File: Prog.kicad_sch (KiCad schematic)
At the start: 26 parts, among them J2 JTAG, J3 microUSB, Q1 MMBT3904, Q2 MMBT3904, U12 CH340G, U25 74LVC245APW, Y1 12M

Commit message: RC
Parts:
- removed C21: 2u2, stdpads:C_0603, symbol Device:C_Small
- removed Q2: MMBT3904, stdpads:SOT-23, symbol Transistor_BJT:MMBT3904
- removed R13, R14, R8: 1k, stdpads:R_0603, symbol Device:R_Small
- removed R9: 10k, stdpads:R_0603, symbol Device:R_Small
- removed U25: 74LVC245APW, stdpads:TSSOP-20_4.4x6.5mm_P0.65mm, symbol GW_Logic:74245
- J3: footprint stdpads:USB_Micro-B_ShouHan_MicroXNJ -> stdpads:USB_Micro-B_Amphenol_10118192-0001
- renumbered R2 to R20, R2 to R23
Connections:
- net JTAG~{OE} is gone; now on an unnamed net: Q1.3 (C)
- net TCKru is gone; now on net UTCK: R20.1
- net UTDI is gone; now on net TDI: U12.13 (~{DTR})
- net UTDO is gone; now on net TDO: U12.9 (~{CTS})
- net UTMS is gone; now on net TMS: U12.14 (~{RTS})
- net +3V3: now also U12.3 (RXD)
- net at R10.2, R11.1: now also Q1.1 (B)
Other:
- company: (none) -> Garrett's Workshop
- title: (none) -> WarpSE (GW4410A)
- moved on the sheet: C23, C25, R20

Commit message: RC
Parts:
- J2: footprint Connector:Tag-Connect_TC2050-IDC-FP_2x05_P1.27mm_Vertical -> stdpads:Tag-Connect_TC2050-IDC-FP_2x05_P1.27mm_Vertical
- J3: LCSC Part C404969 -> C132564
- R10, R11: LCSC Part (none) -> C21190
- R15, R16: value 10k -> DNP; LCSC Part C25804 -> (none)
- R19: LCSC Part (none) -> C23182
- Y1: LCSC Part (none) -> C9002
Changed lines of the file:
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@@
   (title_block
     (title "WarpSE (GW4410A)")
-    (date "2024-03-27")
+    (date "2024-04-23")
     (rev "1.0")
     (company "Garrett's Workshop")
@@
       (effects (font (size 1.27 1.27)))
     )
-    (property "Footprint" "Connector:Tag-Connect_TC2050-IDC-FP_2x05_P1.27mm_Vertical" (at 107.95 57.15 0)
-      (effects (font (size 1.27 1.27)) hide)
-    )
-    (property "Datasheet" "~" (at 107.95 57.15 0)
+    (property "Footprint" "stdpads:Tag-Connect_TC2050-IDC-FP_2x05_P1.27mm_Vertical" (at 107.95 57.15 0)
+      (effects (font (size 1.27 1.27)) hide)
+    )
+    (property "Datasheet" "" (at 107.95 57.15 0)
       (effects (font (size 1.27 1.27)) hide)
     )
@@
       (effects (font (size 1.27 1.27)) (justify left) hide)
     )
-    (property "Datasheet" "http://www.datasheet5.com/pdf-local-2195953" (at 229.87 39.37 0)
+    (property "Datasheet" "" (at 229.87 39.37 0)
       (effects (font (size 1.27 1.27)) hide)
     )
@@
       (effects (font (size 1.27 1.27)) hide)
     )
-    (property "Datasheet" "~" (at 209.55 143.51 0)
+    (property "Datasheet" "" (at 209.55 143.51 0)
       (effects (font (size 1.27 1.27)) hide)
     )
@@
       (effects (font (size 1.27 1.27)) hide)
     )
-    (property "Datasheet" "~" (at 219.71 143.51 0)
+    (property "Datasheet" "" (at 219.71 143.51 0)
       (effects (font (size 1.27 1.27)) hide)
     )
@@
       (effects (font (size 1.27 1.27)) hide)
     )
-    (property "Datasheet" "~" (at 229.87 143.51 0)
+    (property "Datasheet" "" (at 229.87 143.51 0)
       (effects (font (size 1.27 1.27)) hide)
     )
@@
       (effects (font (size 1.27 1.27)) hide)
     )
-    (property "Datasheet" "~" (at 240.03 72.39 0)
+    (property "Datasheet" "" (at 240.03 72.39 0)
       (effects (font (size 1.27 1.27)) hide)
     )
@@
       (effects (font (size 1.27 1.27)) hide)
     )
-    (property "Datasheet" "~" (at 250.19 72.39 0)
+    (property "Datasheet" "" (at 250.19 72.39 0)
       (effects (font (size 1.27 1.27)) hide)
     )
@@
       (effects (font (size 1.27 1.27)) hide)
     )
-    (property "Datasheet" "~" (at 255.27 58.42 0)
-      (effects (font (size 1.27 1.27)) hide)
-    )
-    (property "LCSC Part" "C404969" (at 259.08 57.15 0)
+    (property "Datasheet" "" (at 255.27 58.42 0)
+      (effects (font (size 1.27 1.27)) hide)
+    )
+    (property "LCSC Part" "C132564" (at 259.08 57.15 0)
       (effects (font (size 1.27 1.27)) hide)
     )
@@
       (effects (font (size 1.27 1.27)) (justify right))
     )
-    (property "Value" "10k" (at 73.66 62.23 0)
+    (property "Value" "DNP" (at 73.66 62.23 0)
       (effects (font (size 1.27 1.27)) (justify right))
     )
@@
       (effects (font (size 1.27 1.27)) hide)
     )
-    (property "Datasheet" "~" (at 72.39 60.96 0)
-      (effects (font (size 1.27 1.27)) hide)
-    )
-    (property "LCSC Part" "C25804" (at 72.39 60.96 0)
+    (property "Datasheet" "" (at 72.39 60.96 0)
+      (effects (font (size 1.27 1.27)) hide)
+    )
+    (property "LCSC Part" "" (at 72.39 60.96 0)
       (effects (font (size 1.27 1.27)) hide)
     )
@@
       (effects (font (size 1.27 1.27)) (justify right))
     )
-    (property "Value" "10k" (at 73.66 54.61 0)
+    (property "Value" "DNP" (at 73.66 54.61 0)
       (effects (font (size 1.27 1.27)) (justify right))
     )
@@
       (effects (font (size 1.27 1.27)) hide)
     )
-    (property "Datasheet" "~" (at 72.39 53.34 0)
-      (effects (font (size 1.27 1.27)) hide)
-    )
-    (property "LCSC Part" "C25804" (at 72.39 53.34 0)
+    (property "Datasheet" "" (at 72.39 53.34 0)
+      (effects (font (size 1.27 1.27)) hide)
+    )
+    (property "LCSC Part" "" (at 72.39 53.34 0)
       (effects (font (size 1.27 1.27)) hide)
     )
@@
       (effects (font (size 1.27 1.27)) hide)
     )
-    (property "Datasheet" "~" (at 240.03 102.87 0)
-      (effects (font (size 1.27 1.27)) hide)
-    )
-    (property "LCSC Part" "" (at 240.03 102.87 0)
+    (property "Datasheet" "" (at 240.03 102.87 0)
+      (effects (font (size 1.27 1.27)) hide)
+    )
+    (property "LCSC Part" "C21190" (at 240.03 102.87 0)
       (effects (font (size 1.27 1.27)) hide)
     )
@@
       (effects (font (size 1.27 1.27)) hide)
     )
-    (property "Datasheet" "~" (at 234.95 67.31 0)
+    (property "Datasheet" "" (at 234.95 67.31 0)
+      (effects (font (size 1.27 1.27)) hide)
+    )
+    (property "LCSC Part" "C9002" (at 234.95 67.31 90)
       (effects (font (size 1.27 1.27)) hide)
     )
@@
       (effects (font (size 1.27 1.27) italic) (justify left) hide)
     )
-    (property "Datasheet" "https://www.onsemi.com/pub/Collateral/2N3903-D.PDF" (at 224.79 105.41 0)
+    (property "Datasheet" "" (at 224.79 105.41 0)
       (effects (font (size 1.27 1.27)) (justify left) hide)
     )
@@
       (effects (font (size 1.27 1.27)) hide)
     )
-    (property "Datasheet" "~" (at 198.12 49.53 0)
+    (property "Datasheet" "" (at 198.12 49.53 0)
       (effects (font (size 1.27 1.27)) hide)
     )
@@
       (effects (font (size 1.27 1.27)) hide)
     )
-    (property "Datasheet" "~" (at 222.25 97.79 0)
-      (effects (font (size 1.27 1.27)) hide)
-    )
-    (property "LCSC Part" "" (at 222.25 97.79 0)
+    (property "Datasheet" "" (at 222.25 97.79 0)
+      (effects (font (size 1.27 1.27)) hide)
+    )
+    (property "LCSC Part" "C23182" (at 222.25 97.79 0)
       (effects (font (size 1.27 1.27)) hide)
     )
@@
       (effects (font (size 1.27 1.27)) hide)
     )
-    (property "Datasheet" "~" (at 199.39 143.51 0)
+    (property "Datasheet" "" (at 199.39 143.51 0)
       (effects (font (size 1.27 1.27)) hide)
     )
@@
       (effects (font (size 1.27 1.27)) hide)
     )
-    (property "Datasheet" "~" (at 95.25 52.07 0)
+    (property "Datasheet" "" (at 95.25 52.07 0)
       (effects (font (size 1.27 1.27)) hide)
     )
@@
       (effects (font (size 1.27 1.27)) hide)
     )
-    (property "Datasheet" "~" (at 240.03 107.95 0)
-      (effects (font (size 1.27 1.27)) hide)
-    )
-    (property "LCSC Part" "" (at 240.03 107.95 0)
+    (property "Datasheet" "" (at 240.03 107.95 0)
+      (effects (font (size 1.27 1.27)) hide)
+    )
+    (property "LCSC Part" "C21190" (at 240.03 107.95 0)
       (effects (font (size 1.27 1.27)) hide)
     )
@@
       (effects (font (size 1.27 1.27)) hide)
     )
-    (property "Datasheet" "~" (at 80.01 60.96 0)
-      (effects (font (size 1.27 1.27)) hide)
-    )
+    (property "Datasheet" "" (at 80.01 60.96 0)
+      (effects (font (size 1.27 1.27)) hide)
+    )

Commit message: USB power
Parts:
- added D1: 1N5819, symbol Device:D_Schottky_Small_Filled
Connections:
- net USB5V: now also D1.2 (A)
- new net +5V: D1.1 (K)

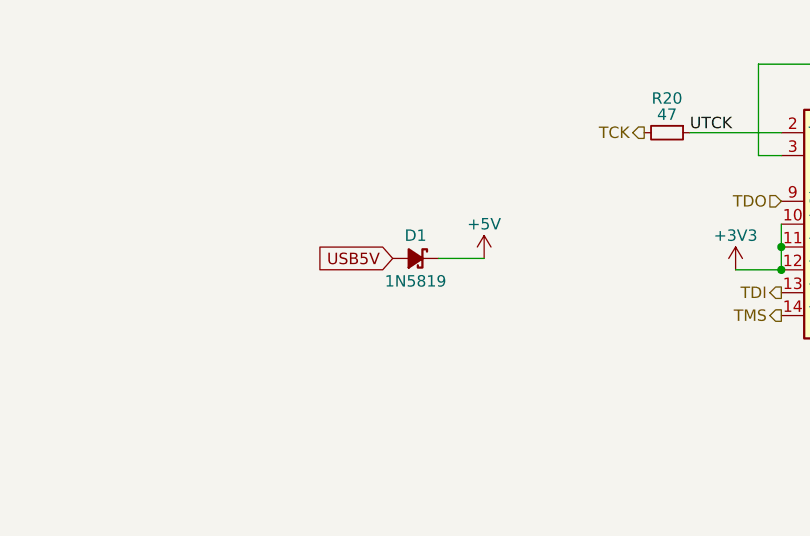
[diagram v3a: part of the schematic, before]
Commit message: Add LM66100 instead of MAX40200AUK
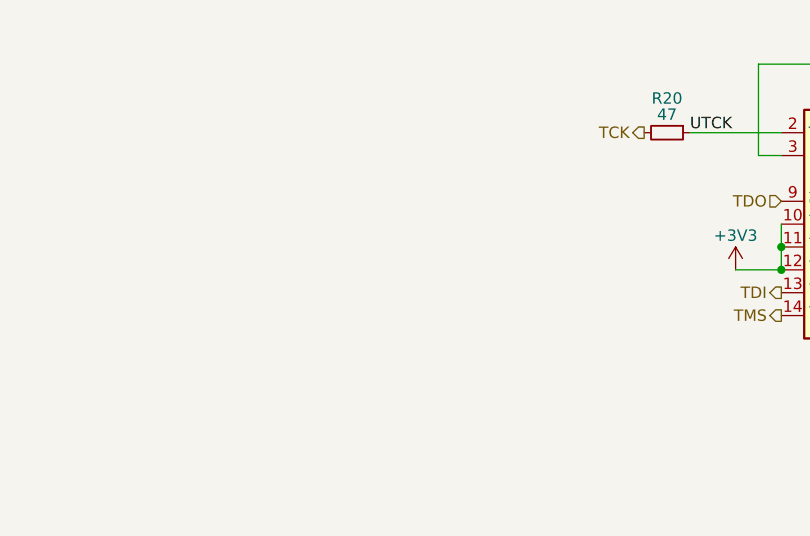
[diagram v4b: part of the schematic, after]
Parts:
- removed D1: 1N5819, symbol Device:D_Schottky_Small_Filled
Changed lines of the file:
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@@
-	(wire
-		(pts
-			(xy 172.72 63.5) (xy 177.8 63.5)
-		)
-		(stroke
-			(width 0)
-			(type default)
-		)
-	)
 	(wire
 		(pts
@@
 	(global_label "USB5V"
 		(shape input)
-		(at 167.64 63.5 180)
-		(fields_autoplaced yes)
-		(effects
-			(font
-				(size 1.27 1.27)
-			)
-			(justify right)
-		)
-		(property "Intersheetrefs" "${INTERSHEET_REFS}"
-			(at 159.2803 63.5 0)
-			(effects
-				(font
-					(size 1.27 1.27)
-				)
-				(justify right)
-				(hide yes)
-			)
-		)
-	)
-	(global_label "USB5V"
-		(shape input)
 		(at 228.6 139.7 180)
 		(fields_autoplaced yes)
@@
 	)
 	(symbol
-		(lib_id "Device:D_Schottky_Small_Filled")
-		(at 170.18 63.5 0)
-		(mirror y)
-		(unit 1)
-		(exclude_from_sim no)
-		(in_bom yes)
-		(on_board yes)
-		(dnp no)
-		(property "Reference" "D1"
-			(at 170.18 60.96 0)
-			(effects
-				(font
-					(size 1.27 1.27)
-				)
-			)
-		)
-		(property "Value" "1N5819"
-			(at 170.18 66.04 0)
-			(effects
-				(font
-					(size 1.27 1.27)
-				)
-			)
-		)
-		(property "Footprint" ""
-			(at 170.18 63.5 90)
-			(effects
-				(font
-					(size 1.27 1.27)
-				)
-				(hide yes)
-			)
-		)
-		(property "Datasheet" "~"
-			(at 170.18 63.5 90)
-			(effects
-				(font
-					(size 1.27 1.27)
-				)
-				(hide yes)
-			)
-		)
-		(property "Description" "Schottky diode, small symbol, filled shape"
-			(at 170.18 63.5 0)
-			(effects
-				(font
-					(size 1.27 1.27)
-				)
-				(hide yes)
-			)
-		)
-		(pin "2"
-		)
-		(pin "1"
-		)
-		(instances
-			(project ""
-				(path "/a5be2cb8-c68d-4180-8412-69a6b4c5b1d4/00000000-0000-0000-0000-000061aa52c4"
-					(reference "D1")
-					(unit 1)
-				)
-			)
-		)
-	)
-	(symbol
 		(lib_id "Device:Crystal_GND24_Small")
 		(at 234.95 67.31 90)
@@
 					(unit 1)
 				)
-			)
-		)
-	)
-	(symbol
-		(lib_id "power:+5V")
-		(at 177.8 63.5 0)
-		(unit 1)
-		(exclude_from_sim no)
-		(in_bom yes)
-		(on_board yes)
-		(dnp no)
-		(property "Reference" "#PWR031"
-			(at 177.8 67.31 0)
-			(effects
-				(font
-					(size 1.27 1.27)
-				)
-				(hide yes)
-			)
-		)
-		(property "Value" "+5V"
-			(at 177.8 59.69 0)
-			(effects
-				(font
-					(size 1.27 1.27)
-				)
-			)
-		)
-		(property "Footprint" ""
-			(at 177.8 63.5 0)
-			(effects
-				(font
-					(size 1.27 1.27)
-				)
-				(hide yes)
-			)
-		)
-		(property "Datasheet" ""
-			(at 177.8 63.5 0)
-			(effects
-				(font
-					(size 1.27 1.27)
-				)
-				(hide yes)
-			)
-		)
-		(property "Description" "Power symbol creates a global label with name \"+5V\""
-			(at 177.8 63.5 0)
-			(effects
-				(font
-					(size 1.27 1.27)
-				)
-				(hide yes)
-			)
-		)
-		(pin "1"
-		)
-		(instances
-			(project ""
-				(path "/a5be2cb8-c68d-4180-8412-69a6b4c5b1d4/00000000-0000-0000-0000-000061aa52c4"
-					(reference "#PWR031")
-					(unit 1)
-				)

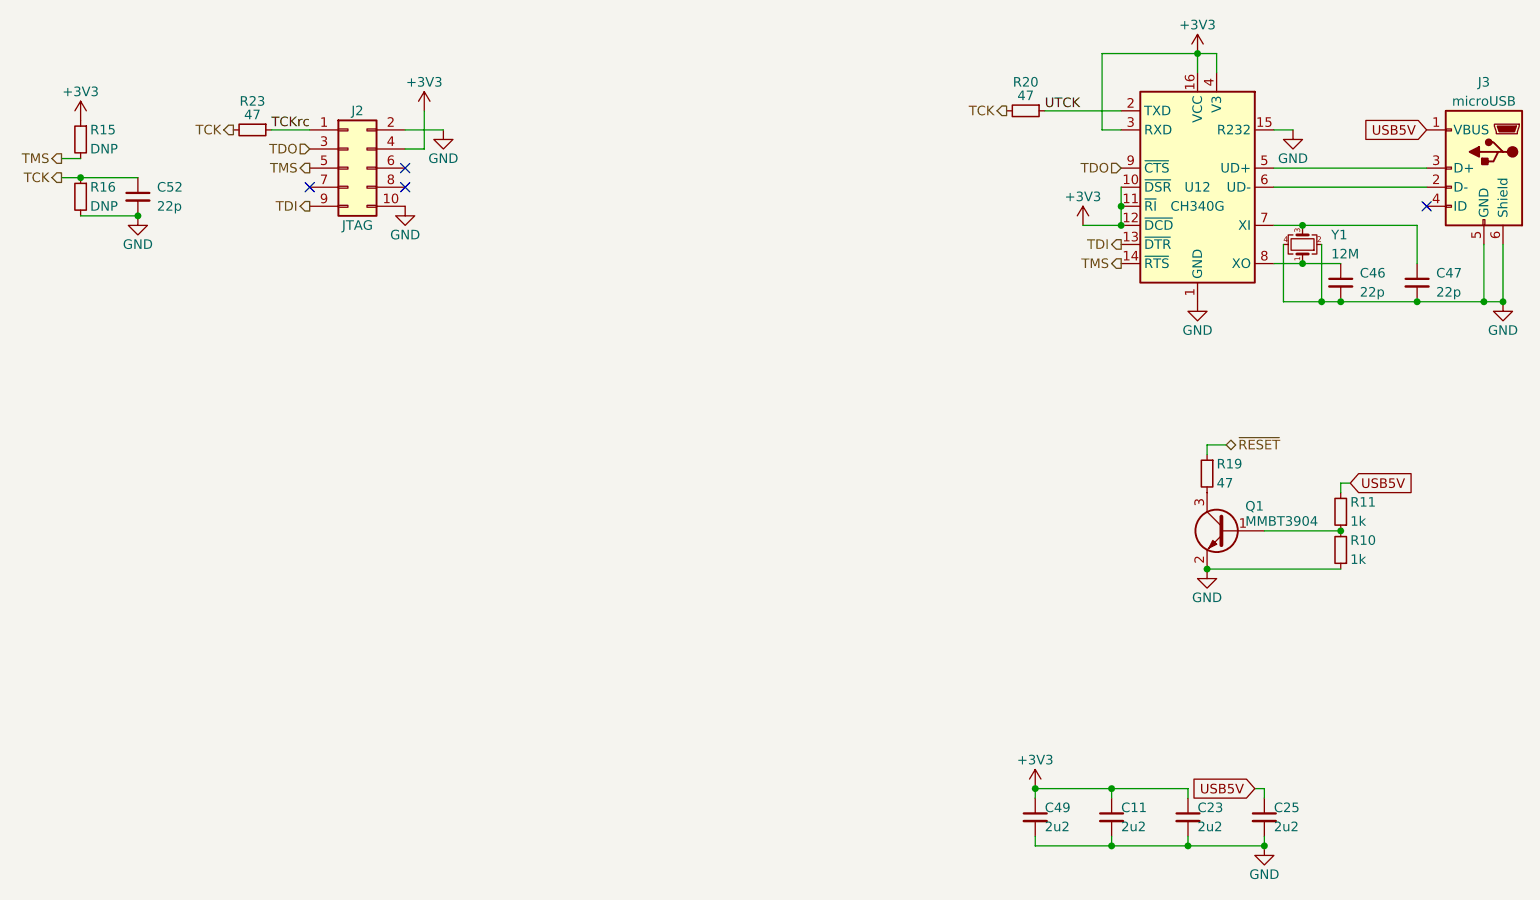
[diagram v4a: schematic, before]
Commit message: Board prerelease revision 3 with USB power, A[23:20] remapping
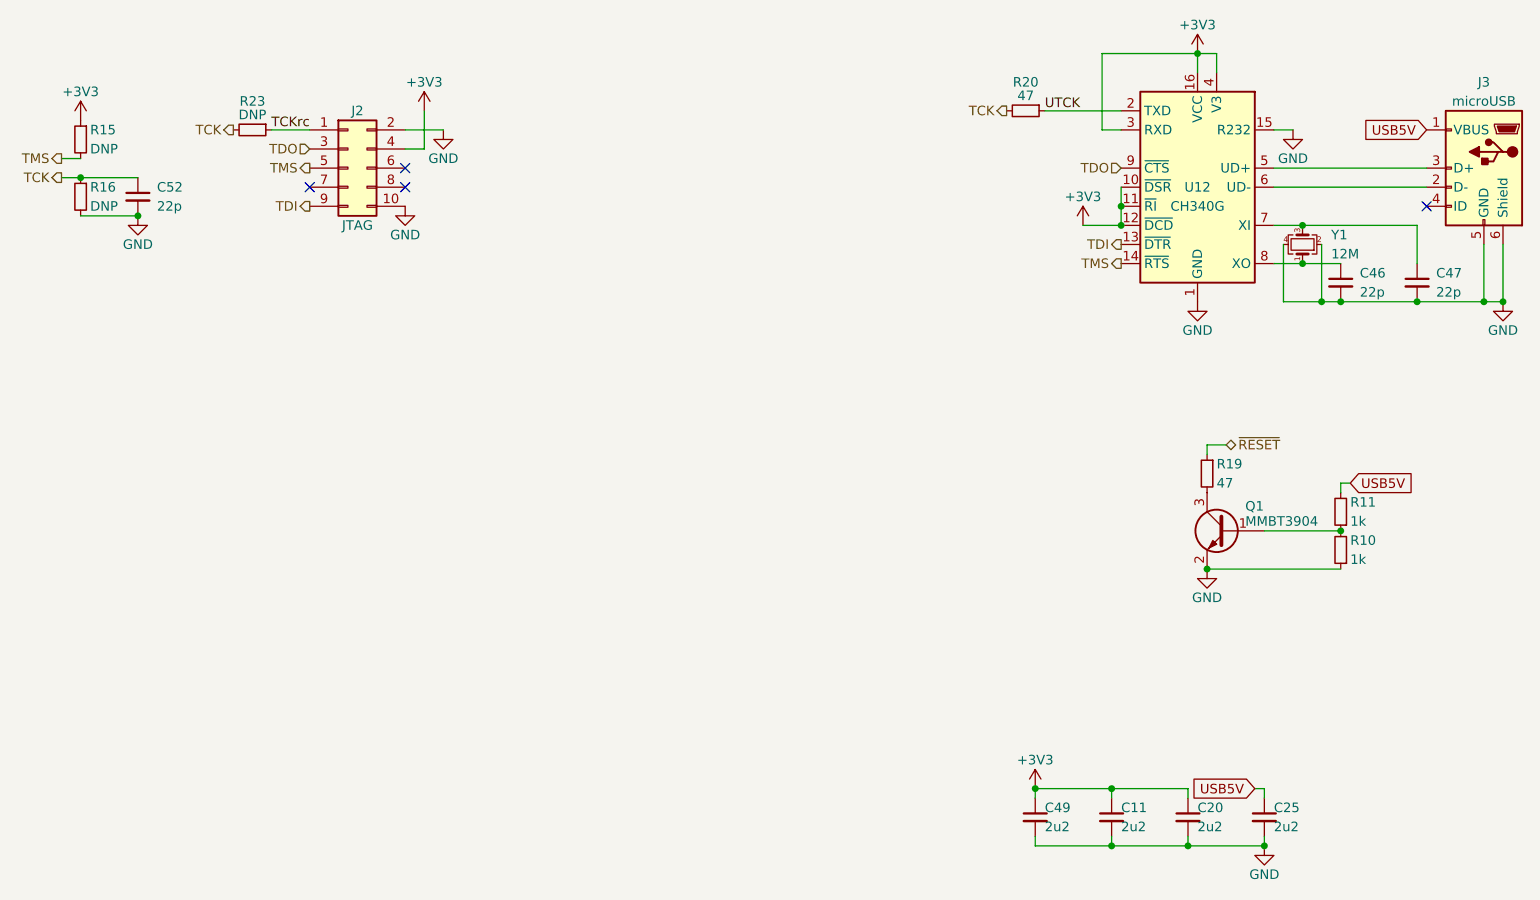
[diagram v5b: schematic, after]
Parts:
- removed C23: 2u2, stdpads:C_0603, symbol Device:C_Small
- added C20: 2u2, stdpads:C_0603, symbol Device:C_Small
- R23: value 47 -> DNP; LCSC Part C23182 -> (none)
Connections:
- net +3V3: now also C20.1
- net GND: now also C20.2
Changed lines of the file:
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@@
-	(symbol
-		(lib_id "Device:C_Small")
-		(at 219.71 143.51 0)
-		(unit 1)
-		(exclude_from_sim no)
-		(in_bom yes)
-		(on_board yes)
-		(dnp no)
-		(property "Reference" "C23"
-			(at 220.98 142.24 0)
-			(effects
-				(font
-					(size 1.27 1.27)
-				)
-				(justify left)
-			)
-		)
-		(property "Value" "2u2"
-			(at 220.98 144.78 0)
-			(effects
-				(font
-					(size 1.27 1.27)
-				)
-				(justify left)
-			)
-		)
-		(property "Footprint" "stdpads:C_0603"
-			(at 219.71 143.51 0)
-			(effects
-				(font
-					(size 1.27 1.27)
-				)
-				(hide yes)
-			)
-		)
-		(property "Datasheet" ""
-			(at 219.71 143.51 0)
-			(effects
-				(font
-					(size 1.27 1.27)
-				)
-				(hide yes)
-			)
-		)
-		(property "Description" ""
-			(at 219.71 143.51 0)
-			(effects
-				(font
-					(size 1.27 1.27)
-				)
-				(hide yes)
-			)
-		)
-		(property "LCSC Part" "C23630"
-			(at 219.71 143.51 0)
-			(effects
-				(font
-					(size 1.27 1.27)
-				)
-				(hide yes)
-			)
-		)
-		(pin "1"
-		)
-		(pin "2"
-		)
-		(instances
-			(project "WarpSE"
-				(path "/a5be2cb8-c68d-4180-8412-69a6b4c5b1d4/00000000-0000-0000-0000-000061aa52c4"
-					(reference "C23")
-					(unit 1)
-				)
-			)
-		)
-	)
 	(symbol
 		(lib_id "Device:C_Small")
@@
 			)
 		)
-		(property "Value" "47"
+		(property "Value" "DNP"
 			(at 95.25 50.8 90)
 			(effects
@@
 			)
 		)
-		(property "LCSC Part" "C23182"
+		(property "LCSC Part" ""
 			(at 95.25 52.07 0)
 			(effects
@@
 					(unit 1)
 				)
+			)
+		)
+	)
+	(symbol
+		(lib_id "Device:C_Small")
+		(at 219.71 143.51 0)
+		(unit 1)
+		(exclude_from_sim no)
+		(in_bom yes)
+		(on_board yes)
+		(dnp no)
+		(property "Reference" "C20"
+			(at 220.98 142.24 0)
+			(effects
+				(font
+					(size 1.27 1.27)
+				)
+				(justify left)
+			)
+		)
+		(property "Value" "2u2"
+			(at 220.98 144.78 0)
+			(effects
+				(font
+					(size 1.27 1.27)
+				)
+				(justify left)
+			)
+		)
+		(property "Footprint" "stdpads:C_0603"
+			(at 219.71 143.51 0)
+			(effects
+				(font
+					(size 1.27 1.27)
+				)
+				(hide yes)
+			)
+		)
+		(property "Datasheet" ""
+			(at 219.71 143.51 0)
+			(effects
+				(font
+					(size 1.27 1.27)
+				)
+				(hide yes)
+			)
+		)
+		(property "Description" ""
+			(at 219.71 143.51 0)
+			(effects
+				(font
+					(size 1.27 1.27)
+				)
+				(hide yes)
+			)
+		)
+		(property "LCSC Part" "C23630"
+			(at 219.71 143.51 0)
+			(effects
+				(font
+					(size 1.27 1.27)
+				)
+				(hide yes)
+			)
+		)
+		(pin "1"
+		)
+		(pin "2"
+		)
+		(instances
+			(project "WarpSE"
+				(path "/a5be2cb8-c68d-4180-8412-69a6b4c5b1d4/00000000-0000-0000-0000-000061aa52c4"
+					(reference "C20")
+					(unit 1)
+				)
